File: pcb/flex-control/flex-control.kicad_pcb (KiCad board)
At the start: 2 copper layers, 1 part, among them J1 Conn_01x06_MountingPin

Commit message: Finish routing
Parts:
- added C1: 22u, Capacitor_SMD:C_0805_2012Metric, F.Cu at (114.9, 103.3)
- added C10: 100n, Capacitor_SMD:C_0402_1005Metric, F.Cu at (92.5, 102.0)
- added C11: 10p, Capacitor_SMD:C_0402_1005Metric, F.Cu at (91.1, 99.9)
- added C12: 10p, Capacitor_SMD:C_0402_1005Metric, F.Cu at (88.8, 97.3)
- added C2: 22u, Capacitor_SMD:C_0603_1608Metric, F.Cu at (114.7, 106.6)
- added C3: 10u, Capacitor_SMD:C_0603_1608Metric, F.Cu at (89.8, 105.4)
- added C4: 100n, Capacitor_SMD:C_0402_1005Metric, F.Cu at (89.3, 104.1)
- added C5: 10u, Capacitor_SMD:C_0603_1608Metric, F.Cu at (104.3, 106.4)
- added C6: 100n, Capacitor_SMD:C_0402_1005Metric, F.Cu at (93.5, 103.0)
- added C7: 100n, Capacitor_SMD:C_0402_1005Metric, F.Cu at (102.6, 107.4)
- added C8: 100n, Capacitor_SMD:C_0402_1005Metric, F.Cu at (103.4, 97.4)
- added C9: 100n, Capacitor_SMD:C_0402_1005Metric, F.Cu at (96.4, 95.8)
- added J2: USB_C_Receptacle_USB2.0_16P, Connector_USB:USB_C_Receptacle_GCT_USB4105-xx-A_16P_TopMnt_Horizontal, F.Cu at (120.8, 101.6)
- added J3: Conn_ARM_SWD_TagConnect_TC2030-NL, Connector:Tag-Connect_TC2030-IDC-NL_2x03_P1.27mm_Vertical, F.Cu at (108.0, 97.7)
- added R1: 10k, Resistor_SMD:R_0402_1005Metric, F.Cu at (98.3, 95.8)
- added R2: 1k5, Resistor_SMD:R_0402_1005Metric, F.Cu at (107.2, 100.2)
- added R3: 330, Resistor_SMD:R_0402_1005Metric, F.Cu at (93.3, 98.4)
- added R4: 5k1, Resistor_SMD:R_0402_1005Metric, F.Cu at (116.5, 95.8)
- added R5: 5k1, Resistor_SMD:R_0402_1005Metric, F.Cu at (116.5, 107.4)
- added U1: AMS1117-3.3, Package_TO_SOT_SMD:SOT-223-3_TabPin2, F.Cu at (109.5, 104.4)
- added U2: STM32F103C8Tx, Package_QFP:LQFP-48_7x7mm_P0.5mm, F.Cu at (99.2, 101.6)
- added U3: SRV05-4, Package_TO_SOT_SMD:SOT-23-6, F.Cu at (113.3, 97.8)
- added Y1: 16MHz, Crystal:Crystal_SMD_3225-4Pin_3.2x2.5mm, F.Cu at (91.1, 97.3)
- moved J1 46.1 mm to (87.0, 101.6)
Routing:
- net GND: track 0.00 -> 42.0 mm, vias 0 -> 15
- net +3V3: track 0.00 -> 30.1 mm, vias 0 -> 10
- net +5V: track 0.00 -> 20.9 mm, vias 0 -> 2
- net /USB+: track 0.00 -> 20.5 mm
- net /USB-: track 0.00 -> 19.4 mm
- net /RST: track 0.00 -> 17.6 mm, vias 0 -> 2
- net /SDA: track 0.00 -> 16.7 mm
- net /SCL: track 0.00 -> 15.7 mm
- net /INT: track 0.00 -> 13.0 mm, vias 0 -> 2
- net /SWO: track 0.00 -> 10.2 mm
- net /SWDIO: track 0.00 -> 9.28 mm, vias 0 -> 2
- net /SWCLK: track 0.00 -> 7.43 mm
- net /XTALO: track 0.00 -> 6.74 mm
- net Net-(J2-CC1): track 0.00 -> 6.45 mm, vias 0 -> 2
- net /XTALR: track 0.00 -> 5.69 mm
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- added copper zone on In2.Cu, net +3V3
- added copper zone on In1.Cu, net GND
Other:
- board outline added: 40.6 x 13 mm
- copper layers 2 -> 4

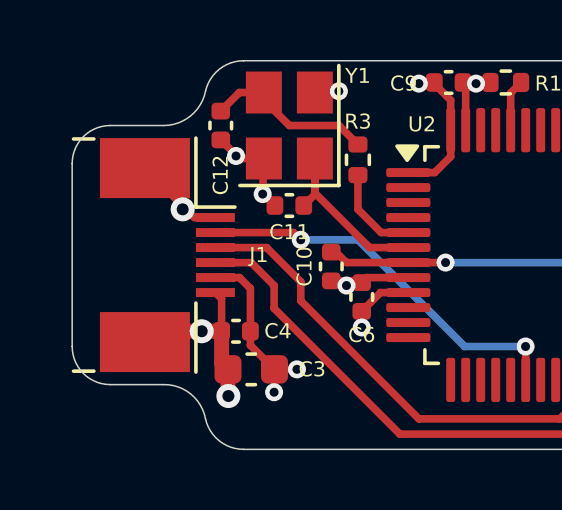
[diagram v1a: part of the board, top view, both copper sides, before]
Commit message: Create production files
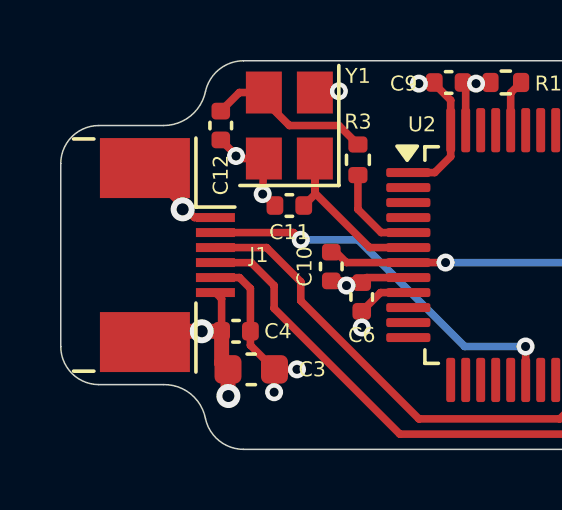
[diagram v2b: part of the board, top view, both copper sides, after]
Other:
- board size 40.6 x 13 mm -> 41 x 13 mm
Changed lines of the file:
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@@
 			)
 		)
-		(property "LCSC" "C15525"
+		(property "LCSC" "C19702"
 			(at 0 0 180)
 			(unlocked yes)
@@
 			)
 		)
-		(property "LCSC" "C15525"
+		(property "LCSC" "C19702"
 			(at 0 0 90)
 			(unlocked yes)
@@
 	)
 	(gr_arc
-		(start 83.82 98.552)
-		(mid 84.191974 97.653974)
-		(end 85.09 97.282)
+		(start 83.439 98.552)
+		(mid 83.810974 97.653974)
+		(end 84.709 97.282)
 		(stroke
 			(width 0.05)
@@
 	)
 	(gr_line
-		(start 85.09 97.282)
+		(start 84.709 97.282)
 		(end 86.868 97.282)
 		(stroke
@@
 	)
 	(gr_line
-		(start 83.82 98.552)
-		(end 83.82 104.648)
+		(start 83.439 98.552)
+		(end 83.439 104.648)
 		(stroke
 			(width 0.05)
@@
 	)
 	(gr_line
-		(start 85.09 105.918)
+		(start 84.709 105.918)
 		(end 86.868 105.918)
 		(stroke
@@
 	)
 	(gr_arc
-		(start 85.09 105.918)
-		(mid 84.191974 105.546026)
-		(end 83.82 104.648)
+		(start 84.709 105.918)
+		(mid 83.810974 105.546026)
+		(end 83.439 104.648)
 		(stroke
 			(width 0.05)
